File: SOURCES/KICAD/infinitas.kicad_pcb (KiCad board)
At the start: 2 copper layers, 240 x 74 mm, 202 parts, among them IC101 PCA9545APW, IC102 CS2100CP, IC103 LCMXO2-1200HC, IC104 TLV62565, IC105 ADM811TARTZ, IC106 LM1117-5.0, IC107 NCP1117LPST33, IC108 NCP1117LPST33, IC109 PCA9545APW, IC201 NC7WZ07, IC202 XE216-512-TQ128, IC203 NCP4681DSQ25T1G, IC204 IS25LP080D, IC701 ADAU1452, IC702 25AA1024, Q701 STD2805, X101 HDR_02x04, X102 IDC_02x32, X103 IDC_02x32, X104 MM-10G, X105 CONN_02X02, X201 USB_B, X202 CONN_01X04, X203 HDR_02x10, X701 HEADER_02X05

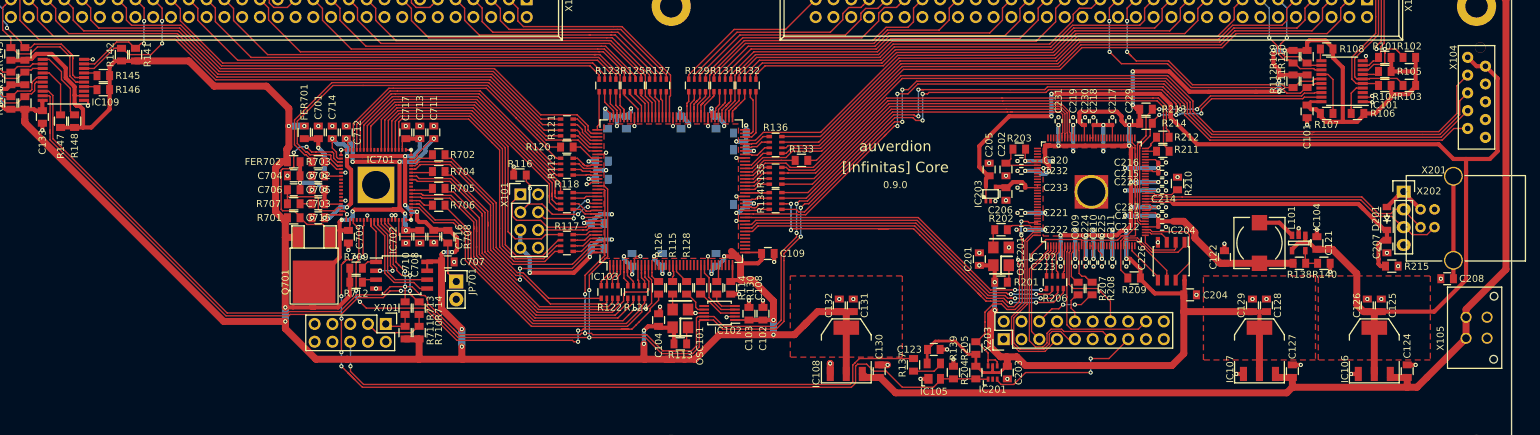
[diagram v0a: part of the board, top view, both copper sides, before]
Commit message: Bugfix on i2c multiplexer
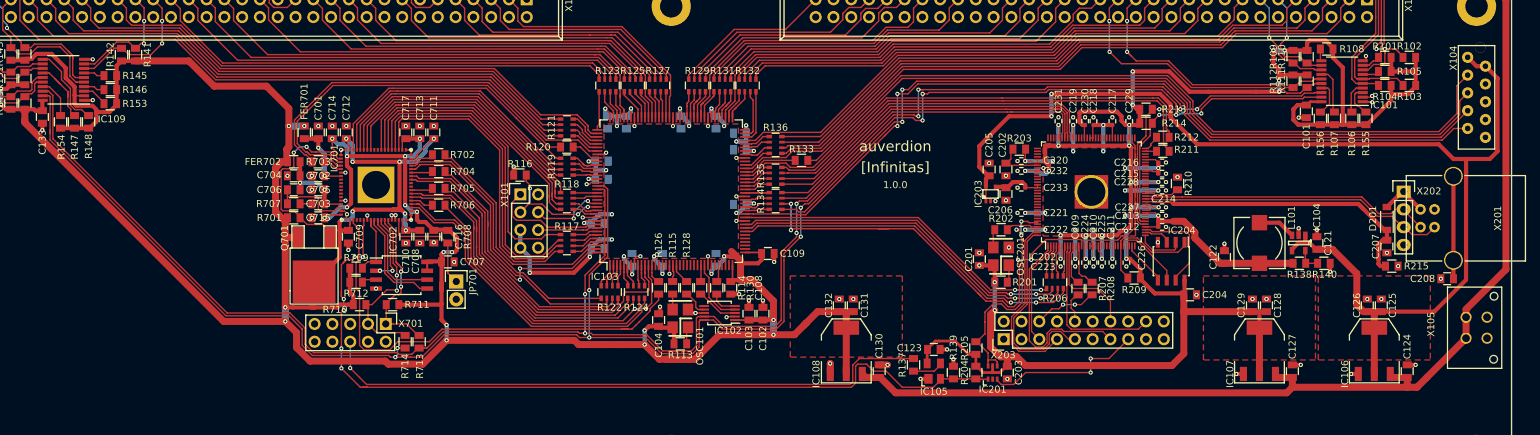
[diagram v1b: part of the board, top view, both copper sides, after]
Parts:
- added R153: RES_47K0_1%_0.125W_Thick_0805, rklib:C0805-RES, F.Cu at (69.9, 48.9)
- added R154: RES_47K0_1%_0.125W_Thick_0805, rklib:C0805-RES, F.Cu at (62.8, 51.5)
- added R155: RES_47K0_1%_0.125W_Thick_0805, rklib:C0805-RES, F.Cu at (249.2, 51.0)
- added R156: RES_47K0_1%_0.125W_Thick_0805, rklib:C0805-RES, F.Cu at (242.7, 51.0)
- C121, C124, C126, C127, C129, C130, C132, C205, C206, C701, C704, C708, C713: value 10u0 -> CAP_10u0_25V_X5R_0805
- C123, C125, C128, C131, C202, C203, C204, C207, C702, C705, C707, C709, C710, C711, C712, C714, C715, C716, C717: value 100n -> CAP_100n_50V_X7R_0805
- C201: value 10n0 -> CAP_10n0_50V_X7R_0805
- C208: value 1n00 -> CAP_1n00_50V_X7R_0805
- D201: footprint Diodes_SMD:SOD-123 -> rklib:SOD123
- IC106, IC107, IC108: footprint TO_SOT_Packages_SMD:SOT-223 -> rklib:SOT223
- IC701: footprint rklib:QFP72_10x10_EP_Handsoldering -> rklib:LFCSP72_10x10_EP_Handsoldering
- JP701: footprint Pin_Headers:Pin_Header_Straight_1x02 -> rklib:HDR_01x02
- Q701: footprint TO_SOT_Packages_SMD:TO-252-2Lead -> rklib:TO252-2Lead
- R139, R215: value 100K -> RES_100K_1%_0.125W_Thick_0805
- R201, R204, R205, R708, R709, R712: value 10K0 -> RES_10K0_1%_0.125W_Thick_0805
- R202, R207, R208, R211, R212: value 33R0 -> 51R0
- R713, R714: value 0R00 -> RES_0R00_1%_0.125W_Thick_0805
- X101: footprint Pin_Headers:Pin_Header_Straight_2x04 -> rklib:HDR_02x04
- X102, X103: footprint Connect:IDC_Header_Straight_64pins -> rklib:IDC64
- X105: footprint Connectors_Molex:Connector_Microfit3_Header_02x02_Straight_43045-0428 -> rklib:Microfit3_43045-0428
- X201: footprint Connect:USB_B -> rklib:USB_B
- X203: footprint Pin_Headers:Pin_Header_Straight_2x10 -> rklib:HDR_02x10
- X701: footprint Pin_Headers:Pin_Header_Straight_2x05 -> rklib:HDR_02x05
- moved R710 9.39 mm to (105.5, 77.6), turned to 0 degrees
- moved R713 5.20 mm to (114.0, 82.9)
- moved R714 5.20 mm to (112.0, 82.9)
- moved R711 4.39 mm to (110.2, 77.6), turned to 180 degrees
- moved R147 2.00 mm to (64.8, 51.5)
- moved R148 2.00 mm to (66.8, 51.5)
- moved R107 1.30 mm to (244.7, 51.0), turned to 270 degrees
- moved R106 1.06 mm to (247.2, 51.0), turned to 270 degrees
- moved R145 1.00 mm to (69.9, 44.9)
- moved R146 1.00 mm to (69.9, 46.9)
- moved C101 0.10 mm to (240.7, 50.0)
- turned C121 to 270 degrees
- turned C123 to 180 degrees
- turned C124 to 270 degrees
- turned C125 to 270 degrees
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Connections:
- C121 pad 1: +5V -> GND
- C121 pad 2: GND -> +5V
- C123 pad 1: VDD -> GND
- C123 pad 2: GND -> VDD
- C124 pad 1: +12V -> GND
- C124 pad 2: GND -> +12V
- C125 pad 1: +5V -> GND
- C125 pad 2: GND -> +5V
- C126 pad 1: +5V -> GND
- C126 pad 2: GND -> +5V
- C127 pad 1: +12V -> GND
- C127 pad 2: GND -> +12V
- C128 pad 1: VDD -> GND
- C128 pad 2: GND -> VDD
- C129 pad 1: VDD -> GND
- C129 pad 2: GND -> VDD
- C130 pad 1: +12V -> GND
- C130 pad 2: GND -> +12V
- C131 pad 1: +3V3 -> GND
- C131 pad 2: GND -> +3V3
- C132 pad 1: +3V3 -> GND
- C132 pad 2: GND -> +3V3
- C201 pad 1: VDD -> GND
- C201 pad 2: GND -> VDD
- C202 pad 1: GND -> Net-(C202-Pad1)
- C202 pad 2: Net-(C202-Pad2) -> GND
- C203 pad 1: VDD -> GND
- C203 pad 2: GND -> VDD
- C204 pad 1: VDD -> GND
- C204 pad 2: GND -> VDD
- C205 pad 1: +5V -> GND
- C205 pad 2: GND -> +5V
- C206 pad 1: +2V5 -> GND
- C206 pad 2: GND -> +2V5
- C207 pad 1: /UAC2 Interface/VBUS -> GND
- C207 pad 2: GND -> /UAC2 Interface/VBUS
- C208 pad 1: Net-(C208-Pad1) -> GND
- C208 pad 2: GND -> Net-(C208-Pad2)
- C701 pad 1: Net-(C701-Pad1) -> GND
- C701 pad 2: GND -> Net-(C701-Pad2)
- C702 pad 1: Net-(C701-Pad1) -> GND
- C702 pad 2: GND -> Net-(C701-Pad2)
- C704 pad 1: Net-(C703-Pad1) -> GND
- C704 pad 2: GND -> Net-(C703-Pad1)
- C705 pad 1: Net-(C703-Pad1) -> GND
- C705 pad 2: GND -> Net-(C703-Pad1)
- C707 pad 1: +3V3 -> GND
- C707 pad 2: GND -> +3V3
- C708 pad 1: VPP -> GND
- C708 pad 2: GND -> VPP
- C709 pad 1: VPP -> GND
- C709 pad 2: GND -> VPP
- C710 pad 1: VPP -> GND
- C710 pad 2: GND -> VPP
- C711 pad 1: VPP -> GND
- C711 pad 2: GND -> VPP
- C712 pad 1: VPP -> GND
- C712 pad 2: GND -> VPP
- C713 pad 1: +3V3 -> GND
- C713 pad 2: GND -> +3V3
- C714 pad 1: +3V3 -> GND
- C714 pad 2: GND -> +3V3
- C715 pad 1: +3V3 -> GND
- C715 pad 2: GND -> +3V3
- C716 pad 1: +3V3 -> GND
- C716 pad 2: GND -> +3V3
- C717 pad 1: +3V3 -> GND
- C717 pad 2: GND -> +3V3
- FER701 pad 2: Net-(C701-Pad1) -> Net-(C701-Pad2)
- IC101 pad 17: (no net) -> Net-(IC101-Pad17)
- IC101 pad 3: (no net) -> Net-(IC101-Pad3)
- IC109 pad 17: (no net) -> Net-(IC109-Pad17)
- IC109 pad 3: (no net) -> Net-(IC109-Pad3)
- IC202 pad 103: Net-(C202-Pad2) -> Net-(C202-Pad1)
- IC701 pad 30: /SDA -> Net-(IC701-Pad30)
- IC701 pad 31: /SCL -> Net-(IC701-Pad31)
- IC701 pad 7: Net-(C701-Pad1) -> Net-(C701-Pad2)
- R139 pad 1: /~RST -> GND
- R139 pad 2: GND -> /~RST
- R201 pad 1: VDD -> Net-(OSC201-Pad1)
- R201 pad 2: Net-(OSC201-Pad1) -> VDD
- R203 pad 1: Net-(C202-Pad2) -> Net-(C202-Pad1)
- R204 pad 1: VDD -> /~RST
- R204 pad 2: /~RST -> VDD
- R205 pad 1: VDD -> /UAC2 Interface/RST_N
- R205 pad 2: /UAC2 Interface/RST_N -> VDD
- R215 pad 1: /UAC2 Interface/VBUS -> GND
- R215 pad 2: GND -> /UAC2 Interface/VBUS
- R708 pad 1: +3V3 -> Net-(IC701-Pad34)
- R708 pad 2: Net-(IC701-Pad34) -> +3V3
- R709 pad 1: Net-(IC701-Pad26) -> +3V3
- R709 pad 2: +3V3 -> Net-(IC701-Pad26)
- R710 pad 2: Net-(R710-Pad2) -> Net-(IC701-Pad30)
- R711 pad 2: Net-(R711-Pad2) -> Net-(IC701-Pad31)
- R712 pad 1: Net-(IC702-Pad3) -> +3V3
- R712 pad 2: +3V3 -> Net-(IC702-Pad3)
- R713 pad 1: Net-(R711-Pad2) -> /SCL
- R713 pad 2: /SCL -> Net-(IC701-Pad31)
- R714 pad 1: Net-(R710-Pad2) -> /SDA
- R714 pad 2: /SDA -> Net-(IC701-Pad30)
- X201 pad 5: Net-(C208-Pad1) -> Net-(C208-Pad2)
- X701 pad 1: Net-(R711-Pad2) -> Net-(IC701-Pad31)
- X701 pad 3: Net-(R710-Pad2) -> Net-(IC701-Pad30)
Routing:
- net Net-(IC701-Pad30): track 0.00 -> 25.0 mm, vias 0 -> 2
- net Net-(IC701-Pad31): track 0.00 -> 23.2 mm, vias 0 -> 2
- net Net-(C208-Pad2): track 0.00 -> 15.3 mm
- net Net-(C208-Pad1): track 15.3 -> 0.00 mm
- net /SCL: track 299.1 -> 286.4 mm, vias 11 -> 9
- net Net-(C701-Pad2): track 0.00 -> 10.0 mm, vias 0 -> 2
- net Net-(C701-Pad1): track 10.0 -> 0.00 mm, vias 2 -> 0
- net Net-(R710-Pad2): track 9.89 -> 0.00 mm
- net /SDA: track 295.1 -> 285.9 mm, vias 12 -> 11
- net +3V3: track 499.1 -> 506.3 mm
- net Net-(C202-Pad2): track 7.10 -> 0.00 mm
- net Net-(C202-Pad1): track 0.00 -> 7.10 mm
- net Net-(IC109-Pad17): track 0.00 -> 5.72 mm
- net VDD: track 305.3 -> 310.6 mm
- net Net-(R711-Pad2): track 5.11 -> 0.00 mm
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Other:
- board text added: "1.0.0"
- board text added: "[Infinitas]"
- board text removed: "0.9.0"
- board text removed: "[Infinitas] Core"

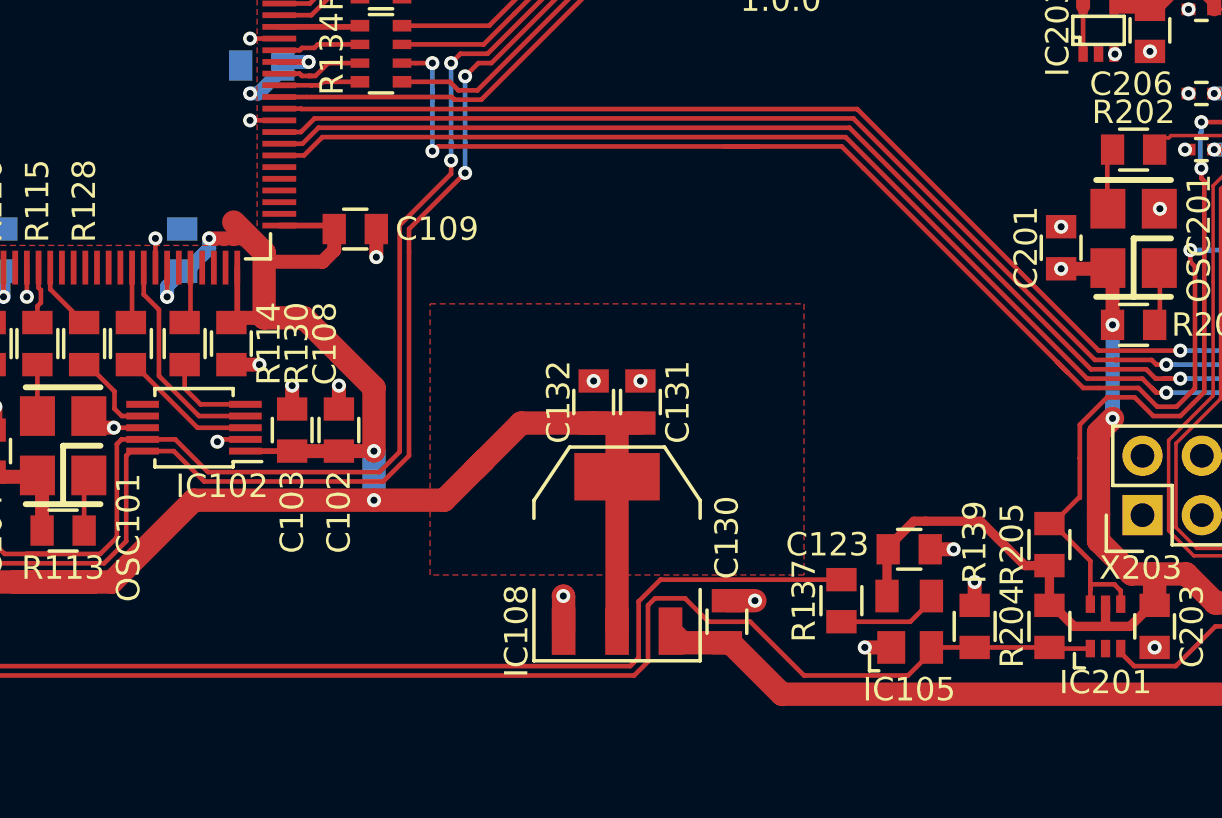
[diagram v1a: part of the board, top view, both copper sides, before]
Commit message: Reset forwarded to FPGA
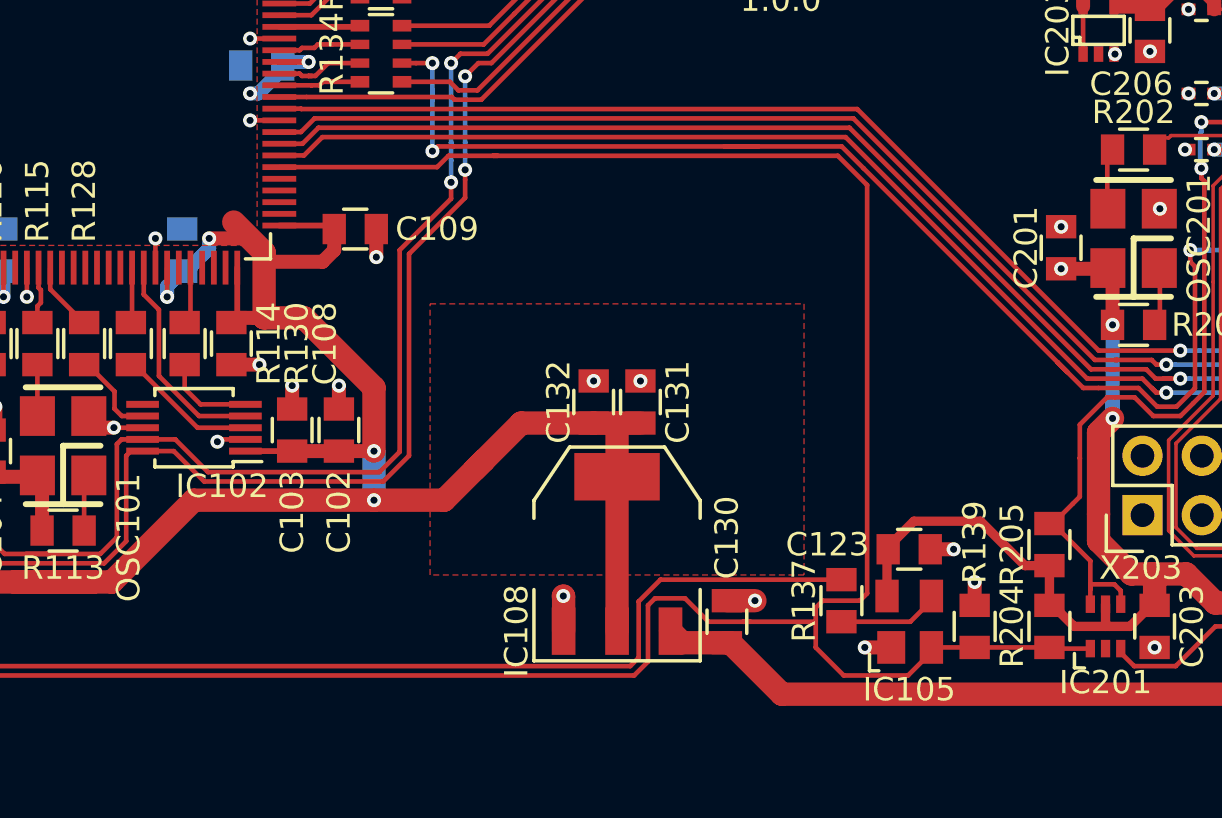
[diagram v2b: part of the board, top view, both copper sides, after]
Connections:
- IC103 pad 42: (no net) -> /~RST
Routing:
- net /~RST: track 124.1 -> 171.6 mm

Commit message: Changed USBi connector
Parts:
- added R315: DNP, rklib:C0805-RES, F.Cu at (108.3, 79.4)
- added R316: DNP, rklib:C0805-RES, F.Cu at (115.6, 85.4)
- added R317: RES_0R00_1%_0.125W_Thick_0805, rklib:C0805-RES, F.Cu at (99.1, 83.1)
- added R318: RES_0R00_1%_0.125W_Thick_0805, rklib:C0805-RES, F.Cu at (103.6, 87.5)
- C123: renamed from C122; value 22u0 -> CAP_22u0_10V_X5R_0805
- C209, C210, C211, C212, C213, C214, C215, C216, C217, C218, C219, C220, C221, C222, C223, C224, C225, C226, C227, C228, C229, C230, C231, C232, C233: value 100n -> CAP_100n_10V_X7R_0402
- C303: renamed from C703; value 5n60 -> CAP_5n60_50V_X7R_0805
- C306: renamed from C706; value 150p -> CAP_150p_50V_C0G_0805
- D201: value MBR120VLSFT -> DIO_MBR120VLSFT
- FER301: renamed from FER701; value 600R./100MHz -> FER_600R_600MA_0805
- FER302: renamed from FER702; value 600R./100MHz -> FER_600R_600MA_0805
- IC101: renamed from IC102; value CS2100CP -> IC_CS2100CP
- IC102: renamed from IC109; value PCA9545APW -> IC_PCA9545APW
- IC103: renamed from IC101; value PCA9545APW -> IC_PCA9545APW
- IC104: renamed from IC103; value LCMXO2-1200HC -> IC_LCMXO2-1200HC-6TG144C
- IC105: renamed from IC104; value TLV62565 -> IC_TLV62565
- IC106: renamed from IC105; value ADM811TARTZ -> IC_ADM811TARTZ
- IC107: renamed from IC106; value LM1117-5.0 -> IC_LM1117MP-5.0
- IC108: renamed from IC107; value NCP1117LPST33 -> IC_NCP1117LPST33
- IC109: renamed from IC108; value NCP1117LPST33 -> IC_NCP1117LPST33
- IC201: renamed from IC202; value XE216-512-TQ128 -> IC_XE216-512-TQ128
- IC202: renamed from IC203; value NCP4681DSQ25T1G -> IC_NCP4681DSQ25T1G
- IC203: renamed from IC204; value IS25LP080D -> IC_IS25LP080D
- IC204: renamed from IC201; value NC7WZ07 -> IC_NC7WZ07
- IC301: renamed from IC701; value ADAU1452 -> IC_ADAU1452
- IC302: renamed from IC702; value 25AA1024 -> IC_25AA1024
- JP301: renamed from JP701; value Jumper -> CON_JUMPER
- L101: value 2u20 -> IND_2U20_30%_4A5
- OSC101: value 24MHz576 -> OSC_24M576
- OSC201: value 24M0 -> OSC_24M0
- Q301: renamed from Q701; value STD2805 -> Q_STD2805
- R119: renamed from R117; value 51R0 -> RES_51R0_5%_4x0603
- R120: renamed from R118; value 51R0 -> RES_51R0_5%_4x0603
- R121: renamed from R119; value 51R0 -> RES_51R0_5%_4x0603
- R122: renamed from R120; value 51R0 -> RES_51R0_1%_0.125W_Thick_0805
- R123: renamed from R121; value 51R0 -> RES_51R0_5%_4x0603
- R138: renamed from R122; value 51R0 -> RES_51R0_5%_4x0603
- R139: renamed from R123; value 51R0 -> RES_51R0_5%_4x0603
- R140: renamed from R124; value 51R0 -> RES_51R0_5%_4x0603
- R141: renamed from R125; value 51R0 -> RES_51R0_5%_4x0603
- R143: renamed from R127; value 51R0 -> RES_51R0_5%_4x0603
- R145: renamed from R129; value 51R0 -> RES_51R0_5%_4x0603
- R147: renamed from R131; value 51R0 -> RES_51R0_5%_4x0603
- R148: renamed from R132; value 51R0 -> RES_51R0_5%_4x0603
- R150: renamed from R134; value 51R0 -> RES_51R0_5%_4x0603
- R151: renamed from R135; value 51R0 -> RES_51R0_5%_4x0603
- R152: renamed from R136; value 51R0 -> RES_51R0_5%_4x0603
- R153: renamed from R137; value 1K00 -> RES_1K00_1%_0.125W_Thick_0805
- R154: renamed from R138; value 80K6 -> RES_80K6_1%_0.125W_Thick_0805
- R156: renamed from R140; value 120K -> RES_120K_1%_0.125W_Thick_0805
- R202: value 51R0 -> RES_51R0_1%_0.125W_Thick_0805
- R203: value 4R70 -> RES_4R70_1%_0.125W_Thick_0805
- R204: renamed from R206; value 51R0 -> RES_51R0_5%_4x0603
- R205: renamed from R207; value 51R0 -> RES_51R0_1%_0.125W_Thick_0805
- R206: renamed from R208; value 51R0 -> RES_51R0_1%_0.125W_Thick_0805
- R207: renamed from R209; value 1K00 -> RES_1K00_1%_0.125W_Thick_0805
- R208: renamed from R210; value 43R2 -> RES_43R2_1%_0.125W_Thick_0805
- R209: renamed from R211; value 51R0 -> RES_51R0_1%_0.125W_Thick_0805
- R210: renamed from R212; value 51R0 -> RES_51R0_1%_0.125W_Thick_0805
- R301: renamed from R701; value 1K00 -> RES_1K00_1%_0.125W_Thick_0805
- R302: renamed from R702; value 51R0 -> RES_51R0_1%_0.125W_Thick_0805
- R303: renamed from R703; value 51R0 -> RES_51R0_1%_0.125W_Thick_0805
- R304: renamed from R704; value 51R0 -> RES_51R0_1%_0.125W_Thick_0805
- R305: renamed from R705; value 51R0 -> RES_51R0_1%_0.125W_Thick_0805
- R306: renamed from R706; value 51R0 -> RES_51R0_1%_0.125W_Thick_0805
- R307: renamed from R707; value 4K32 -> RES_4K32_1%_0.125W_Thick_0805
- X101: value HDR_02x04 -> CON_HDR_02x04
- X102, X103: value IDC_02x32 -> CON_IDC64
- X104: value MM-10G -> CON_MicroMatch-10G
- X105: value CONN_02X02 -> CON_MicroFit3_02x02
- X201: renamed from X203; value HDR_02x10 -> CON_HDR_02x10
- X202: renamed from X201; value USB_B -> CON_USB_B
- X203: renamed from X202; value CONN_01X04 -> CON_HDR_01x04
- X301: renamed from X701; value HEADER_02X05 -> CON_HDR_02x05
- moved R309 10.3 mm to (115.6, 79.4), turned to 180 degrees
- moved R310 5.40 mm to (115.6, 77.4)
- moved B104 4.00 mm to (35.0, 95.0)
- moved B105 4.00 mm to (150.0, 95.0)
- moved B106 4.00 mm to (265.0, 95.0)
- moved R312 3.90 mm to (115.6, 81.4), turned to 180 degrees
- moved X301 3.40 mm to (112.1, 82.2)
- moved R311 1.68 mm to (115.6, 83.4), turned to 180 degrees
- turned R156 to 180 degrees
- turned R208 to 270 degrees
- renumbered B104 to B103, B105 to B104, B106 to B105, B108 to B106, C133 to C101, C101 to C105, C105 to C106, C106 to C107, C107 to C108, C108 to C109, C109 to C110, C110 to C111, C111 to C112, C112 to C113, C113 to C114, C114 to C115, C115 to C116, C116 to C117, C117 to C118, C118 to C119, C119 to C120, C120 to C121, C121 to C122, C123 to C124, C124 to C125, C125 to C126, C126 to C127, C127 to C128, C128 to C129, C129 to C130, C130 to C131, C131 to C132, C132 to C133, C204 to C203, C203 to C204, C701 to C301, C702 to C302, C704 to C304, C705 to C305, C707 to C307, C708 to C308, C709 to C309, C710 to C310, C711 to C311, C712 to C312, C713 to C313, C714 to C314, C715 to C315, C716 to C316, C717 to C317, R113 to R101, R141 to R102, R142 to R103, R143 to R104, R144 to R105, R145 to R106, R146 to R107, R153 to R108, R154 to R109, R147 to R110, R148 to R111, R149 to R112, R150 to R113, R151 to R114, R152 to R115, R114 to R116, R115 to R117, R116 to R118, R101 to R124, R102 to R125, R103 to R126, R104 to R127, R105 to R128, R106 to R129, R155 to R130, R156 to R131, R107 to R132, R108 to R133, R111 to R134, R112 to R135, R109 to R136, R110 to R137, R126 to R142, R128 to R144, R130 to R146, R133 to R149, R139 to R155, R213 to R211, R214 to R212, R204 to R213, R205 to R214, R708 to R308, R710 to R309, R711 to R310, R713 to R311, R714 to R312, R709 to R313, R712 to R314
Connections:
- IC105 pad 5: Net-(IC104-Pad5) (its old number) -> Net-(IC105-Pad5)
- IC201 pad 48: Net-(IC202-Pad48) -> Net-(IC201-Pad48)
- IC301 pad 32: GND -> /DSP/MOSI
- IC301 pad 33: GND -> /DSP/~SS
- R154 pad 2: Net-(IC104-Pad5) (its old number) -> Net-(IC105-Pad5)
- R156 pad 1: Net-(IC104-Pad5) (its old number) -> GND
- R156 pad 2: GND -> Net-(IC105-Pad5)
- R208 pad 1: Net-(IC202-Pad48) -> GND
- R208 pad 2: GND -> Net-(IC201-Pad48)
- X301 pad 5: (no net) -> /DSP/MISO
- X301 pad 7: (no net) -> /DSP/SCLK
- X301 pad 8: (no net) -> /DSP/MOSI
- X301 pad 9: (no net) -> /DSP/~SS
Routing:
- net /DSP/MOSI: track 0.00 -> 29.2 mm, vias 0 -> 2
- net /DSP/~SS: track 0.00 -> 27.7 mm, vias 0 -> 2
- net /MCLK: track 66.7 -> 88.5 mm, vias 0 -> 4
- net /~RST: track 171.6 -> 182.7 mm, vias 6 -> 8
- net /DSP/SCLK: track 0.00 -> 11.0 mm
- net /SCL: track 286.4 -> 293.2 mm
- net Net-(IC301-Pad31): track 23.2 -> 29.6 mm
- net /SDA: track 285.9 -> 291.9 mm
- net /~USBRST: track 88.1 -> 82.3 mm, vias 1 -> 2
- net Net-(IC202-Pad48): track 4.97 -> 0.00 mm
- net Net-(IC201-Pad48): track 0.00 -> 4.97 mm
- net +3V3: track 506.3 -> 510.7 mm
- net Net-(IC105-Pad5): track 0.00 -> 3.52 mm
- net Net-(IC104-Pad5) (its old number): track 3.52 -> 0.00 mm
- net /DSP/MISO: track 0.00 -> 2.96 mm
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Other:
- board size 240 x 74 mm -> 240 x 70 mm
